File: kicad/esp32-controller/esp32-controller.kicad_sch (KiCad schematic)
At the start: 39 parts, among them J1 RJ45, J2 RJ45, J3 RJ45, J4 RJ45, J5 RJ45, J6 RJ45, J7 Barrel_Jack_Switch, J8 Conn_01x04_Pin, U1 SN65LVDS049, U2 SN65LVDS049, U3 SN65LVDS049, U4 74AHC1G08, U5 74AHC1G08, U6 74AHC1G08, U7 ESP32-S3-WROOM-1, U8 AZ1117-3.3

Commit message: Complete controller pcb
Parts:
- removed J1, J3: RJ45, Connector_RJ:RJ45_Amphenol_54602-x08_Horizontal, symbol Connector:RJ45
- removed R1, R2, R3, R4, R5, R6: 100, Resistor_SMD:R_0805_2012Metric, symbol Device:R
- added C10, C11, C12: 4nF, Capacitor_SMD:C_0805_2012Metric, symbol Device:C
- added C7, C8, C9: 100nF, Capacitor_SMD:C_0805_2012Metric, symbol Device:C
- added J4, J6: RJ45, Connector_RJ:RJ45_Amphenol_54602-x08_Horizontal, symbol Connector:RJ45
- added U10, U11, U12: 74AHC1G08, Package_TO_SOT_SMD:SOT-23-5_HandSoldering, symbol 74xGxx:74AHC1G08
- added U7, U8, U9: SN65LVDS049, Package_SO:TSSOP-16_4.4x5mm_P0.65mm, symbol My_New_Library:SN65LVDS049
- renumbered C7 to C13, C8 to C14, C9 to C15, C10 to C16, C11 to C17, J2 to J1, J4 to J2, J6 to J3, R7 to R1, R8 to R2, R9 to R3, U8 to U13, U7 to U14
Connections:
- net +12V: now also J4.5, J4.7, J6.5, J6.7
- net +3V3: now also C10.1, C11.1, C12.1, C7.1, C8.1, C9.1, U10.3 (GND), U11.3 (GND), U12.3 (GND), U7.12 (VCC), U7.16 (EN), U8.12 (VCC), U8.16 (EN), U9.12 (VCC), U9.16 (EN)
- net Cout_N2: no longer J3.3, U3.7 (DOUT1-)
- net Cout_P2: no longer J3.4, U3.8 (DOUT1+)
- net Dout_N2: no longer J3.2, U3.5 (DOUT2-)
- net Dout_P2: no longer J3.1, U3.6 (DOUT2+)
- net GND: now also C10.2, C11.2, C12.2, C7.2, C8.2, C9.2, J4.6, J4.8, J6.6, J6.8, U10.5 (VCC), U11.5 (VCC), U12.5 (VCC), U7.13 (GND), U7.9 (~{EN}), U8.13 (GND), U8.9 (~{EN}), U9.13 (GND), U9.9 (~{EN})
- net MOSI: now also U7.11 (DIN2), U8.11 (DIN2), U9.11 (DIN2)
- net SCK: now also U4.2, U5.2, U6.2, U10.2, U11.2, U12.2; no longer U4.1, U5.1, U6.1
- net CS5: now reaches U14.15 (IO3)
- net CS5: now also U12.1
- net CS4: now reaches U14.17 (IO9)
- net CS4: now also U11.1
- net CS3: now reaches U14.18 (IO10)
- net CS3: now also U10.1
- net CS2: now reaches U14.23 (IO21)
- net CS2: now also U6.1
- net CS1: now reaches U14.24 (IO47)
- net CS1: now also U5.1
- net CS0: now reaches U14.25 (IO48)
- net CS0: now also U4.1
- net Cin_N2 renamed Cout_N5
- net Cout_N5: now also U8.7 (DOUT1-)
- net Cin_P2 renamed Cout_P5
- net Cout_P5: now also U8.8 (DOUT1+)
- net Din_N2 renamed Dout_N5
- net Dout_N5: now also U8.5 (DOUT2-)
- net Din_P2 renamed Dout_P5
- net Dout_P5: now also U8.6 (DOUT2+)
- new net: U11.4, U8.10 (DIN1)
- new net: U12.4, U9.10 (DIN1)
- new net: U10.4, U7.10 (DIN1)
- new net Cout_N3: J3.3, U3.7 (DOUT1-)
- new net Cout_N4: J4.3, U7.7 (DOUT1-)
- new net Cout_N6: J6.3, U9.7 (DOUT1-)
- new net Cout_P3: J3.4, U3.8 (DOUT1+)
- new net Cout_P4: J4.4, U7.8 (DOUT1+)
- new net Cout_P6: J6.4, U9.8 (DOUT1+)
- new net Dout_N3: J3.2, U3.5 (DOUT2-)
- new net Dout_N4: J4.2, U7.5 (DOUT2-)
- new net Dout_N6: J6.2, U9.5 (DOUT2-)
- new net Dout_P3: J3.1, U3.6 (DOUT2+)
- new net Dout_P4: J4.1, U7.6 (DOUT2+)
- new net Dout_P6: J6.1, U9.6 (DOUT2+)
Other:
- moved on the sheet: BOOT1, C1, C13, C14, C15, C16, C17, C2, C3, C4, C5, C6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

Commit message: Fix pcb + software
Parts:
- added TP1, TP2: TestPoint, TestPoint:TestPoint_Pad_D2.0mm, symbol Connector:TestPoint
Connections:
- net +3V3: now also U10.5 (VCC), U11.5 (VCC), U12.5 (VCC), U4.5 (VCC), U5.5 (VCC), U6.5 (VCC); no longer U10.3 (GND), U11.3 (GND), U12.3 (GND), U4.3 (GND), U5.3 (GND), U6.3 (GND)
- net GND: now also U10.3 (GND), U11.3 (GND), U12.3 (GND), U4.3 (GND), U5.3 (GND), U6.3 (GND); no longer U10.5 (VCC), U11.5 (VCC), U12.5 (VCC), U4.5 (VCC), U5.5 (VCC), U6.5 (VCC)
- net at U14.31 (IO38): now also TP1.1
- net at U14.32 (IO39): now also TP2.1

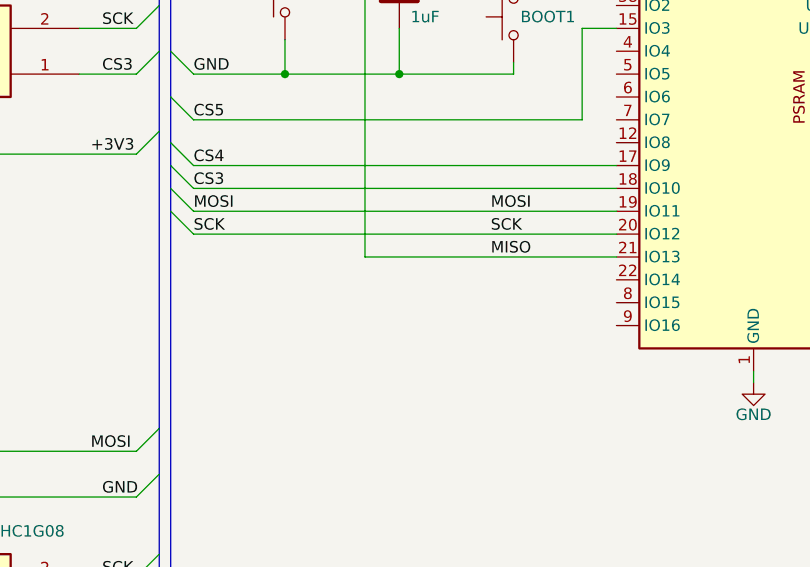
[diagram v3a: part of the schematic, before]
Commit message: Add testpoints to pcbs
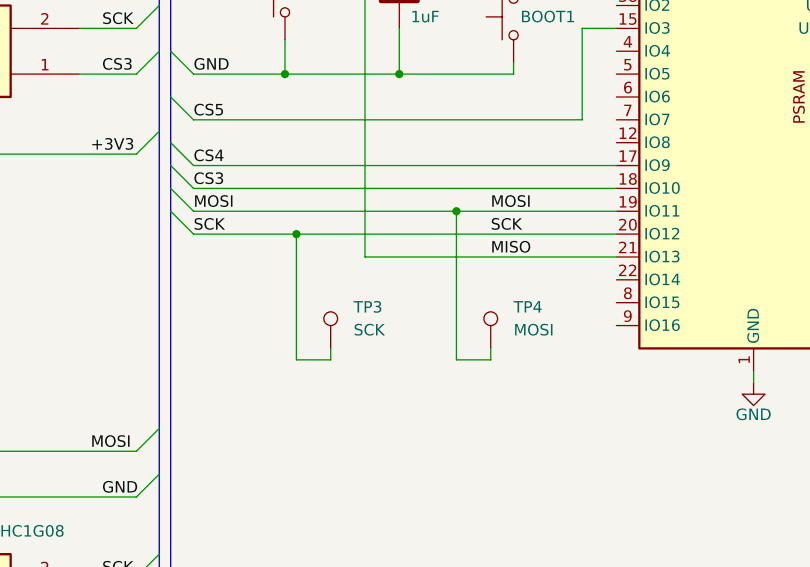
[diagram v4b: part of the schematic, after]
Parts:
- added TP3: SCK, TestPoint:TestPoint_Pad_D1.5mm, symbol Connector:TestPoint
- added TP4: MOSI, TestPoint:TestPoint_Pad_D1.5mm, symbol Connector:TestPoint
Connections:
- net MOSI: now also TP4.1
- net SCK: now also TP3.1
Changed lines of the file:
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@@
 	)
 	(junction
+		(at 287.02 73.66)
+		(diameter 0)
+		(color 0 0 0 0)
+	)
+	(junction
 		(at 308.61 144.78)
 		(diameter 0)
@@
 	)
 	(junction
+		(at 304.8 71.12)
+		(diameter 0)
+		(color 0 0 0 0)
+	)
+	(junction
 		(at 77.47 190.5)
 		(diameter 0)
@@
 	(wire
 		(pts
-			(xy 275.59 71.12) (xy 322.58 71.12)
+			(xy 275.59 71.12) (xy 304.8 71.12)
 		)
 		(stroke
@@
 	(wire
 		(pts
+			(xy 287.02 73.66) (xy 322.58 73.66)
+		)
+		(stroke
+			(width 0)
+			(type default)
+		)
+	)
+	(wire
+		(pts
 			(xy 38.1 110.49) (xy 48.26 110.49)
 		)
@@
 	(wire
 		(pts
+			(xy 308.61 87.63) (xy 304.8 87.63)
+		)
+		(stroke
+			(width 0)
+			(type default)
+		)
+	)
+	(wire
+		(pts
 			(xy 191.77 81.28) (xy 208.28 81.28)
 		)
@@
 	(wire
 		(pts
-			(xy 275.59 73.66) (xy 322.58 73.66)
+			(xy 275.59 73.66) (xy 287.02 73.66)
 		)
 		(stroke
@@
 	(wire
 		(pts
+			(xy 290.83 87.63) (xy 287.02 87.63)
+		)
+		(stroke
+			(width 0)
+			(type default)
+		)
+	)
+	(wire
+		(pts
 			(xy 77.47 81.28) (xy 77.47 82.55)
 		)
@@
 	(wire
 		(pts
+			(xy 287.02 87.63) (xy 287.02 73.66)
+		)
+		(stroke
+			(width 0)
+			(type default)
+		)
+	)
+	(wire
+		(pts
 			(xy 193.04 123.19) (xy 191.77 123.19)
 		)
@@
 	(wire
 		(pts
+			(xy 304.8 71.12) (xy 304.8 87.63)
+		)
+		(stroke
+			(width 0)
+			(type default)
+		)
+	)
+	(wire
+		(pts
 			(xy 237.49 97.79) (xy 228.6 97.79)
 		)
@@
 	(wire
 		(pts
+			(xy 304.8 71.12) (xy 322.58 71.12)
+		)
+		(stroke
+			(width 0)
+			(type default)
+		)
+	)
+	(wire
+		(pts
 			(xy 168.91 168.91) (xy 193.04 168.91)
 		)
@@
 	(wire
 		(pts
+			(xy 308.61 86.36) (xy 308.61 87.63)
+		)
+		(stroke
+			(width 0)
+			(type default)
+		)
+	)
+	(wire
+		(pts
 			(xy 60.96 190.5) (xy 77.47 190.5)
 		)
@@
 	(wire
 		(pts
+			(xy 290.83 86.36) (xy 290.83 87.63)
+		)
+		(stroke
+			(width 0)
+			(type default)
+		)
+	)
+	(wire
+		(pts
 			(xy 336.55 139.7) (xy 341.63 139.7)
 		)
@@
 	)
 	(symbol
+		(lib_id "Connector:TestPoint")
+		(at 308.61 86.36 0)
+		(unit 1)
+		(exclude_from_sim no)
+		(in_bom yes)
+		(on_board yes)
+		(dnp no)
+		(fields_autoplaced yes)
+		(property "Reference" "TP4"
+			(at 311.15 81.7879 0)
+			(effects
+				(font
+					(size 1.27 1.27)
+				)
+				(justify left)
+			)
+		)
+		(property "Value" "MOSI"
+			(at 311.15 84.3279 0)
+			(effects
+				(font
+					(size 1.27 1.27)
+				)
+				(justify left)
+			)
+		)
+		(property "Footprint" "TestPoint:TestPoint_Pad_D1.5mm"
+			(at 313.69 86.36 0)
+			(effects
+				(font
+					(size 1.27 1.27)
+				)
+				(hide yes)
+			)
+		)
+		(property "Datasheet" "~"
+			(at 313.69 86.36 0)
+			(effects
+				(font
+					(size 1.27 1.27)
+				)
+				(hide yes)
+			)
+		)
+		(property "Description" "test point"
+			(at 308.61 86.36 0)
+			(effects
+				(font
+					(size 1.27 1.27)
+				)
+				(hide yes)
+			)
+		)
+		(pin "1"
+		)
+		(instances
+			(project "esp32-controller"
+				(path "/bfb88c66-3278-41a9-b822-09be2f151e4c"
+					(reference "TP4")
+					(unit 1)
+				)
+			)
+		)
+	)
+	(symbol
 		(lib_id "My_New_Library:SN65LVDS049")
 		(at 208.28 105.41 0)
@@
 					(unit 1)
 				)
+			)
+		)
+	)
+	(symbol
+		(lib_id "Connector:TestPoint")
+		(at 290.83 86.36 0)
+		(unit 1)
+		(exclude_from_sim no)
+		(in_bom yes)
+		(on_board yes)
+		(dnp no)
+		(fields_autoplaced yes)
+		(property "Reference" "TP3"
+			(at 293.37 81.7879 0)
+			(effects
+				(font
+					(size 1.27 1.27)
+				)
+				(justify left)
+			)
+		)
+		(property "Value" "SCK"
+			(at 293.37 84.3279 0)
+			(effects
+				(font
+					(size 1.27 1.27)
+				)
+				(justify left)
+			)
+		)
+		(property "Footprint" "TestPoint:TestPoint_Pad_D1.5mm"
+			(at 295.91 86.36 0)
+			(effects
+				(font
+					(size 1.27 1.27)
+				)
+				(hide yes)
+			)
+		)
+		(property "Datasheet" "~"
+			(at 295.91 86.36 0)
+			(effects
+				(font
+					(size 1.27 1.27)
+				)
+				(hide yes)
+			)
+		)
+		(property "Description" "test point"
+			(at 290.83 86.36 0)
+			(effects
+				(font
+					(size 1.27 1.27)
+				)
+				(hide yes)
+			)
+		)
+		(pin "1"
+		)
+		(instances
+			(project ""
+				(path "/bfb88c66-3278-41a9-b822-09be2f151e4c"
+					(reference "TP3")
+					(unit 1)
+				)
